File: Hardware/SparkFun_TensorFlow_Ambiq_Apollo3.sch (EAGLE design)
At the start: 67 parts, among them J5 CORTEX_DEBUG, J7 CAMERA-HIMAX, U2 LIS2DH12, U3 1.8V, U5 ARTEMIS_MODULESMD, Y2 32.768kHz

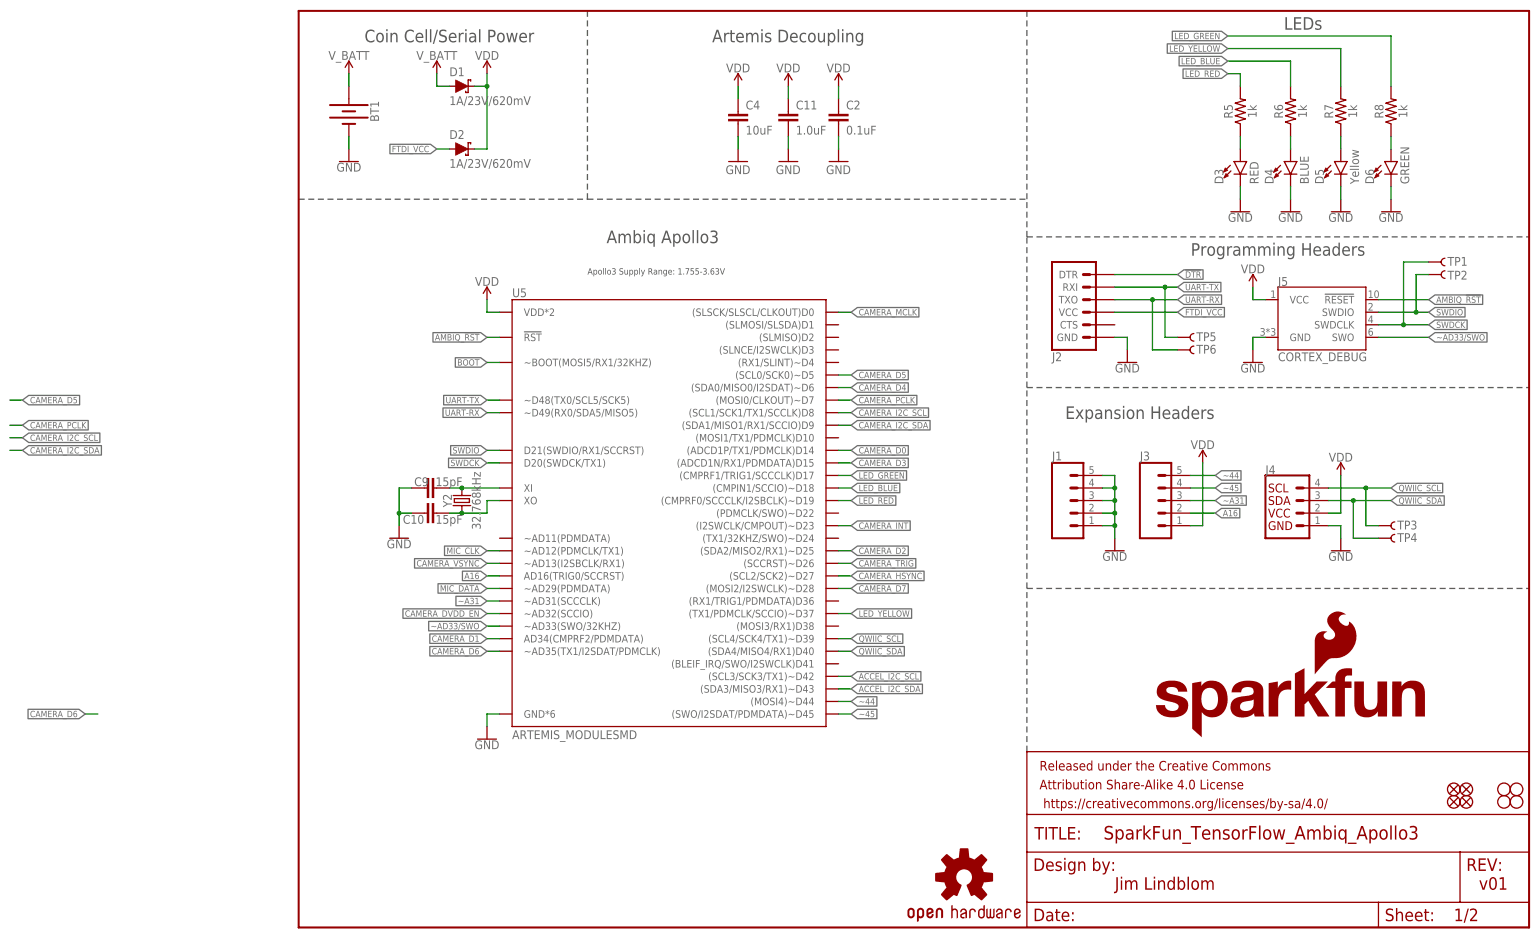
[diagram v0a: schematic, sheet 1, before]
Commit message: Move MCLK to PWM pin.
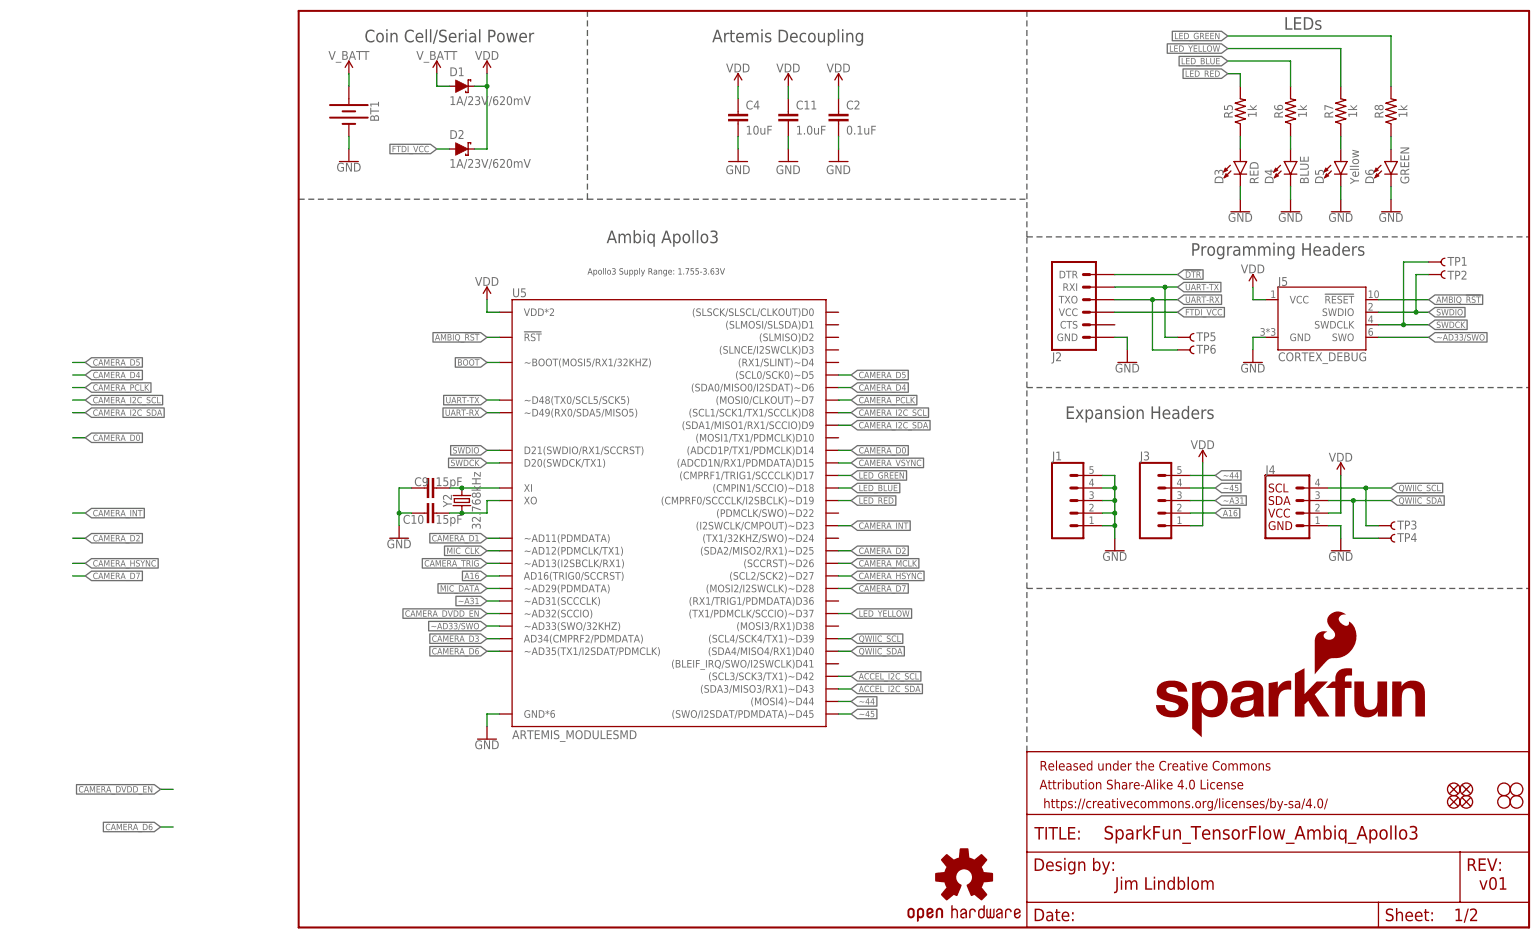
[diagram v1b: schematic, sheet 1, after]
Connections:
- net CAMERA_D1: now also U5.~AD11(PDMDATA); no longer U5.AD34(CMPRF2/PDMDATA)
- net CAMERA_D3: now also U5.AD34(CMPRF2/PDMDATA); no longer U5.(ADCD1N/RX1/PDMDATA)D15
- net CAMERA_MCLK: now also U5.(SCCRST)~D26; no longer U5.(SLSCK/SLSCL/CLKOUT)D0
- net CAMERA_TRIG: now also U5.~AD13(I2SBCLK/RX1); no longer U5.(SCCRST)~D26
- net CAMERA_VSYNC: now also U5.(ADCD1N/RX1/PDMDATA)D15; no longer U5.~AD13(I2SBCLK/RX1)
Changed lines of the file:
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@@
 <pinref part="U5" gate="U1" pin="~AD32(SCCIO)"/>
 </segment>
+<segment>
+<wire x1="-25.4" y1="27.94" x2="-27.94" y2="27.94" width="0.1524" layer="91"/>
+<label x="-27.94" y="27.94" size="1.27" layer="95" rot="R180" xref="yes"/>
+</segment>
 </net>
 <net name="CAMERA_VSYNC" class="0">
 <segment>
-<wire x1="40.64" y1="73.66" x2="38.1" y2="73.66" width="0.1524" layer="91"/>
-<label x="38.1" y="73.66" size="1.27" layer="95" rot="R180" xref="yes"/>
-<pinref part="U5" gate="U1" pin="~AD13(I2SBCLK/RX1)"/>
+<wire x1="109.22" y1="93.98" x2="111.76" y2="93.98" width="0.1524" layer="91"/>
+<label x="111.76" y="93.98" size="1.27" layer="95" xref="yes"/>
+<pinref part="U5" gate="U1" pin="(ADCD1N/RX1/PDMDATA)D15"/>
 </segment>
 </net>
@@
 <pinref part="U5" gate="U1" pin="(I2SWCLK/CMPOUT)~D23"/>
 </segment>
+<segment>
+<wire x1="-45.72" y1="83.82" x2="-43.18" y2="83.82" width="0.1524" layer="91"/>
+<label x="-43.18" y="83.82" size="1.27" layer="95" xref="yes"/>
+</segment>
 </net>
 <net name="CAMERA_I2C_SDA" class="0">
@@
 </segment>
 <segment>
-<wire x1="-58.42" y1="96.52" x2="-55.88" y2="96.52" width="0.1524" layer="91"/>
-<label x="-55.88" y="96.52" size="1.27" layer="95" xref="yes"/>
+<wire x1="-45.72" y1="104.14" x2="-43.18" y2="104.14" width="0.1524" layer="91"/>
+<label x="-43.18" y="104.14" size="1.27" layer="95" xref="yes"/>
 </segment>
 </net>
@@
 </segment>
 <segment>
-<wire x1="-58.42" y1="99.06" x2="-55.88" y2="99.06" width="0.1524" layer="91"/>
-<label x="-55.88" y="99.06" size="1.27" layer="95" xref="yes"/>
+<wire x1="-45.72" y1="106.68" x2="-43.18" y2="106.68" width="0.1524" layer="91"/>
+<label x="-43.18" y="106.68" size="1.27" layer="95" xref="yes"/>
 </segment>
 </net>
@@
 <net name="CAMERA_TRIG" class="0">
 <segment>
-<wire x1="109.22" y1="73.66" x2="111.76" y2="73.66" width="0.1524" layer="91"/>
-<label x="111.76" y="73.66" size="1.27" layer="95" xref="yes"/>
-<pinref part="U5" gate="U1" pin="(SCCRST)~D26"/>
+<wire x1="40.64" y1="73.66" x2="38.1" y2="73.66" width="0.1524" layer="91"/>
+<label x="38.1" y="73.66" size="1.27" layer="95" rot="R180" xref="yes"/>
+<pinref part="U5" gate="U1" pin="~AD13(I2SBCLK/RX1)"/>
 </segment>
 </net>
@@
 <pinref part="U5" gate="U1" pin="(SCL2/SCK2)~D27"/>
 </segment>
+<segment>
+<wire x1="-45.72" y1="73.66" x2="-43.18" y2="73.66" width="0.1524" layer="91"/>
+<label x="-43.18" y="73.66" size="1.27" layer="95" xref="yes"/>
+</segment>
 </net>
 <net name="CAMERA_D7" class="0">
@@
 <pinref part="U5" gate="U1" pin="(MOSI2/I2SWCLK)~D28"/>
 </segment>
+<segment>
+<wire x1="-45.72" y1="71.12" x2="-43.18" y2="71.12" width="0.1524" layer="91"/>
+<label x="-43.18" y="71.12" size="1.27" layer="95" xref="yes"/>
+</segment>
 </net>
 <net name="CAMERA_D6" class="0">
@@
 </segment>
 <segment>
-<wire x1="-40.64" y1="43.18" x2="-43.18" y2="43.18" width="0.1524" layer="91"/>
-<label x="-43.18" y="43.18" size="1.27" layer="95" rot="R180" xref="yes"/>
+<wire x1="-25.4" y1="20.32" x2="-27.94" y2="20.32" width="0.1524" layer="91"/>
+<label x="-27.94" y="20.32" size="1.27" layer="95" rot="R180" xref="yes"/>
 </segment>
 </net>
@@
 </segment>
 <segment>
-<wire x1="-58.42" y1="106.68" x2="-55.88" y2="106.68" width="0.1524" layer="91"/>
-<label x="-55.88" y="106.68" size="1.27" layer="95" xref="yes"/>
+<wire x1="-45.72" y1="114.3" x2="-43.18" y2="114.3" width="0.1524" layer="91"/>
+<label x="-43.18" y="114.3" size="1.27" layer="95" xref="yes"/>
 </segment>
 </net>
@@
 </segment>
 <segment>
-<wire x1="-58.42" y1="101.6" x2="-55.88" y2="101.6" width="0.1524" layer="91"/>
-<label x="-55.88" y="101.6" size="1.27" layer="95" xref="yes"/>
+<wire x1="-45.72" y1="109.22" x2="-43.18" y2="109.22" width="0.1524" layer="91"/>
+<label x="-43.18" y="109.22" size="1.27" layer="95" xref="yes"/>
 </segment>
 </net>
@@
 <pinref part="U5" gate="U1" pin="(SDA0/MISO0/I2SDAT)~D6"/>
 </segment>
+<segment>
+<wire x1="-45.72" y1="111.76" x2="-43.18" y2="111.76" width="0.1524" layer="91"/>
+<label x="-43.18" y="111.76" size="1.27" layer="95" xref="yes"/>
+</segment>
 </net>
 <net name="CAMERA_D0" class="0">
@@
 <pinref part="U5" gate="U1" pin="(ADCD1P/TX1/PDMCLK)D14"/>
 </segment>
+<segment>
+<wire x1="-45.72" y1="99.06" x2="-43.18" y2="99.06" width="0.1524" layer="91"/>
+<label x="-43.18" y="99.06" size="1.27" layer="95" xref="yes"/>
+</segment>
 </net>
 <net name="CAMERA_D3" class="0">
-<segment>
-<wire x1="109.22" y1="93.98" x2="111.76" y2="93.98" width="0.1524" layer="91"/>
-<label x="111.76" y="93.98" size="1.27" layer="95" xref="yes"/>
-<pinref part="U5" gate="U1" pin="(ADCD1N/RX1/PDMDATA)D15"/>
-</segment>
-</net>
-<net name="CAMERA_D1" class="0">
 <segment>
 <wire x1="40.64" y1="58.42" x2="38.1" y2="58.42" width="0.1524" layer="91"/>
@@
 </segment>
 </net>
+<net name="CAMERA_D1" class="0">
+<segment>
+<wire x1="40.64" y1="78.74" x2="38.1" y2="78.74" width="0.1524" layer="91"/>
+<label x="38.1" y="78.74" size="1.27" layer="95" rot="R180" xref="yes"/>
+<pinref part="U5" gate="U1" pin="~AD11(PDMDATA)"/>
+</segment>
+</net>
 <net name="CAMERA_D2" class="0">
 <segment>
@@
 <label x="111.76" y="76.2" size="1.27" layer="95" xref="yes"/>
 <pinref part="U5" gate="U1" pin="(SDA2/MISO2/RX1)~D25"/>
+</segment>
+<segment>
+<wire x1="-45.72" y1="78.74" x2="-43.18" y2="78.74" width="0.1524" layer="91"/>
+<label x="-43.18" y="78.74" size="1.27" layer="95" xref="yes"/>
 </segment>
 </net>
@@
 <net name="CAMERA_MCLK" class="0">
 <segment>
-<wire x1="109.22" y1="124.46" x2="111.76" y2="124.46" width="0.1524" layer="91"/>
-<label x="111.76" y="124.46" size="1.27" layer="95" xref="yes"/>
-<pinref part="U5" gate="U1" pin="(SLSCK/SLSCL/CLKOUT)D0"/>
-</segment>
-</net>
+<wire x1="109.22" y1="73.66" x2="111.76" y2="73.66" width="0.1524" layer="91"/>
+<label x="111.76" y="73.66" size="1.27" layer="95" xref="yes"/>
+<pinref part="U5" gate="U1" pin="(SCCRST)~D26"/>
+</segment>
+</net>

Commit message: Move mics to 2cm spacing. Re-wire camera connection.
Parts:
- S3: device SparkFun-Switches:MOMENTARY-SWITCH-SPST-SMD-5.2MM-TALL -> SparkFun-Switches:MOMENTARY-SWITCH-SPST-SMD-4.6X2.8MM
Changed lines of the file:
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@@
 <grid distance="0.1" unitdist="inch" unit="inch" style="lines" multiple="1" display="no" altdistance="0.01" altunitdist="inch" altunit="inch"/>
 <layers>
-<layer number="1" name="Top" color="4" fill="1" visible="no" active="no"/>
-<layer number="2" name="Route2" color="22" fill="3" visible="no" active="no"/>
-<layer number="3" name="Route3" color="4" fill="3" visible="no" active="no"/>
-<layer number="4" name="Route4" color="1" fill="4" visible="no" active="no"/>
-<layer number="5" name="Route5" color="4" fill="4" visible="no" active="no"/>
-<layer number="6" name="Route6" color="1" fill="8" visible="no" active="no"/>
-<layer number="7" name="Route7" color="4" fill="8" visible="no" active="no"/>
-<layer number="8" name="Route8" color="1" fill="2" visible="no" active="no"/>
-<layer number="9" name="Route9" color="4" fill="2" visible="no" active="no"/>
-<layer number="10" name="Route10" color="1" fill="7" visible="no" active="no"/>
-<layer number="11" name="Route11" color="4" fill="7" visible="no" active="no"/>
-<layer number="12" name="Route12" color="1" fill="5" visible="no" active="no"/>
-<layer number="13" name="Route13" color="4" fill="5" visible="no" active="no"/>
-<layer number="14" name="Route14" color="1" fill="6" visible="no" active="no"/>
-<layer number="15" name="Route15" color="14" fill="6" visible="no" active="no"/>
-<layer number="16" name="Bottom" color="1" fill="1" visible="no" active="no"/>
-<layer number="17" name="Pads" color="2" fill="1" visible="no" active="no"/>
-<layer number="18" name="Vias" color="2" fill="1" visible="no" active="no"/>
-<layer number="19" name="Unrouted" color="6" fill="1" visible="no" active="no"/>
-<layer number="20" name="Dimension" color="24" fill="1" visible="no" active="no"/>
-<layer number="21" name="tPlace" color="16" fill="1" visible="no" active="no"/>
-<layer number="22" name="bPlace" color="14" fill="1" visible="no" active="no"/>
-<layer number="23" name="tOrigins" color="15" fill="1" visible="no" active="no"/>
-<layer number="24" name="bOrigins" color="15" fill="1" visible="no" active="no"/>
-<layer number="25" name="tNames" color="7" fill="1" visible="no" active="no"/>
-<layer number="26" name="bNames" color="7" fill="1" visible="no" active="no"/>
-<layer number="27" name="tValues" color="7" fill="1" visible="no" active="no"/>
-<layer number="28" name="bValues" color="7" fill="1" visible="no" active="no"/>
+<layer number="1" name="Top" color="4" fill="1" visible="yes" active="no"/>
+<layer number="2" name="Route2" color="22" fill="3" visible="yes" active="no"/>
+<layer number="3" name="Route3" color="4" fill="3" visible="yes" active="no"/>
+<layer number="4" name="Route4" color="1" fill="4" visible="yes" active="no"/>
+<layer number="5" name="Route5" color="4" fill="4" visible="yes" active="no"/>
+<layer number="6" name="Route6" color="1" fill="8" visible="yes" active="no"/>
+<layer number="7" name="Route7" color="4" fill="8" visible="yes" active="no"/>
+<layer number="8" name="Route8" color="1" fill="2" visible="yes" active="no"/>
+<layer number="9" name="Route9" color="4" fill="2" visible="yes" active="no"/>
+<layer number="10" name="Route10" color="1" fill="7" visible="yes" active="no"/>
+<layer number="11" name="Route11" color="4" fill="7" visible="yes" active="no"/>
+<layer number="12" name="Route12" color="1" fill="5" visible="yes" active="no"/>
+<layer number="13" name="Route13" color="4" fill="5" visible="yes" active="no"/>
+<layer number="14" name="Route14" color="1" fill="6" visible="yes" active="no"/>
+<layer number="15" name="Route15" color="14" fill="6" visible="yes" active="no"/>
+<layer number="16" name="Bottom" color="1" fill="1" visible="yes" active="no"/>
+<layer number="17" name="Pads" color="2" fill="1" visible="yes" active="no"/>
+<layer number="18" name="Vias" color="2" fill="1" visible="yes" active="no"/>
+<layer number="19" name="Unrouted" color="6" fill="1" visible="yes" active="no"/>
+<layer number="20" name="Dimension" color="24" fill="1" visible="yes" active="no"/>
+<layer number="21" name="tPlace" color="16" fill="1" visible="yes" active="no"/>
+<layer number="22" name="bPlace" color="14" fill="1" visible="yes" active="no"/>
+<layer number="23" name="tOrigins" color="15" fill="1" visible="yes" active="no"/>
+<layer number="24" name="bOrigins" color="15" fill="1" visible="yes" active="no"/>
+<layer number="25" name="tNames" color="7" fill="1" visible="yes" active="no"/>
+<layer number="26" name="bNames" color="7" fill="1" visible="yes" active="no"/>
+<layer number="27" name="tValues" color="7" fill="1" visible="yes" active="no"/>
+<layer number="28" name="bValues" color="7" fill="1" visible="yes" active="no"/>
 <layer number="29" name="tStop" color="7" fill="3" visible="no" active="no"/>
 <layer number="30" name="bStop" color="7" fill="6" visible="no" active="no"/>
@@
 <layer number="35" name="tGlue" color="7" fill="4" visible="no" active="no"/>
 <layer number="36" name="bGlue" color="7" fill="5" visible="no" active="no"/>
-<layer number="37" name="tTest" color="7" fill="1" visible="no" active="no"/>
-<layer number="38" name="bTest" color="7" fill="1" visible="no" active="no"/>
+<layer number="37" name="tTest" color="7" fill="1" visible="yes" active="no"/>
+<layer number="38" name="bTest" color="7" fill="1" visible="yes" active="no"/>
 <layer number="39" name="tKeepout" color="4" fill="11" visible="no" active="no"/>
 <layer number="40" name="bKeepout" color="1" fill="11" visible="no" active="no"/>
@@
 <layer number="44" name="Drills" color="7" fill="1" visible="no" active="no"/>
 <layer number="45" name="Holes" color="7" fill="1" visible="no" active="no"/>
-<layer number="46" name="Milling" color="3" fill="1" visible="no" active="no"/>
-<layer number="47" name="Measures" color="7" fill="1" visible="no" active="no"/>
-<layer number="48" name="Document" color="7" fill="1" visible="no" active="no"/>
-<layer number="49" name="Reference" color="7" fill="1" visible="no" active="no"/>
-<layer number="50" name="dxf" color="7" fill="1" visible="no" active="no"/>
-<layer number="51" name="tDocu" color="6" fill="1" visible="no" active="no"/>
-<layer number="52" name="bDocu" color="7" fill="1" visible="no" active="no"/>
-<layer number="53" name="tGND_GNDA" color="7" fill="9" visible="no" active="no"/>
-<layer number="54" name="bGND_GNDA" color="1" fill="9" visible="no" active="no"/>
-<layer number="56" name="wert" color="7" fill="1" visible="no" active="no"/>
-<layer number="57" name="tCAD" color="7" fill="1" visible="no" active="no"/>
-<layer number="59" name="tCarbon" color="7" fill="1" visible="no" active="no"/>
-<layer number="60" name="bCarbon" color="7" fill="1" visible="no" active="no"/>
+<layer number="46" name="Milling" color="3" fill="1" visible="yes" active="no"/>
+<layer number="47" name="Measures" color="7" fill="1" visible="yes" active="no"/>
+<layer number="48" name="Document" color="7" fill="1" visible="yes" active="no"/>
+<layer number="49" name="Reference" color="7" fill="1" visible="yes" active="no"/>
+<layer number="50" name="dxf" color="7" fill="1" visible="yes" active="no"/>
+<layer number="51" name="tDocu" color="6" fill="1" visible="yes" active="no"/>
+<layer number="52" name="bDocu" color="7" fill="1" visible="yes" active="no"/>
+<layer number="53" name="tGND_GNDA" color="7" fill="9" visible="yes" active="no"/>
+<layer number="54" name="bGND_GNDA" color="1" fill="9" visible="yes" active="no"/>
+<layer number="56" name="wert" color="7" fill="1" visible="yes" active="no"/>
+<layer number="57" name="tCAD" color="7" fill="1" visible="yes" active="no"/>
+<layer number="59" name="tCarbon" color="7" fill="1" visible="yes" active="no"/>
+<layer number="60" name="bCarbon" color="7" fill="1" visible="yes" active="no"/>
 <layer number="88" name="SimResults" color="9" fill="1" visible="yes" active="yes"/>
 <layer number="89" name="SimProbes" color="9" fill="1" visible="yes" active="yes"/>
@@
 <part name="U5" library="Testing" deviceset="ARTEMIS_MODULE" device="SMD"/>
 <part name="E1" library="SparkFun-Sensors" deviceset="SPH0641LM4H-1_MICROPHONE" device="" value="SPH0641LM4H-1"/>
-<part name="S3" library="SparkFun-Switches" deviceset="MOMENTARY-SWITCH-SPST" device="-SMD-5.2MM-TALL" value="RESET"/>
+<part name="S3" library="SparkFun-Switches" deviceset="MOMENTARY-SWITCH-SPST" device="-SMD-4.6X2.8MM" value="RESET"/>
 <part name="R27" library="SparkFun-Resistors" deviceset="100KOHM" device="-0603-1/10W-1%" value="100k"/>
 <part name="C6" library="SparkFun-Capacitors" deviceset="0.1UF" device="-0603-25V-5%" value="0.1uF"/>

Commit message: Move cap to avoid silk
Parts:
- U5: device Testing:ARTEMIS_MODULESMD -> SparkFun-IC-Microcontroller:ARTEMIS_MODULESMD
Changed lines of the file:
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@@
 <part name="TP6" library="SparkFun-Connectors" deviceset="TEST-POINT" device="3X5"/>
 <part name="TP7" library="SparkFun-Connectors" deviceset="TEST-POINT" device="3X5"/>
-<part name="U5" library="Testing" deviceset="ARTEMIS_MODULE" device="SMD"/>
+<part name="U5" library="SparkFun-IC-Microcontroller" deviceset="ARTEMIS_MODULE" device="SMD"/>
 <part name="E1" library="SparkFun-Sensors" deviceset="SPH0641LM4H-1_MICROPHONE" device="" value="SPH0641LM4H-1"/>
 <part name="S3" library="SparkFun-Switches" deviceset="MOMENTARY-SWITCH-SPST" device="-SMD-4.6X2.8MM" value="RESET"/>
